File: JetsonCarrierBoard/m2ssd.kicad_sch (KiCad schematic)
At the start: 0 parts

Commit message: Finished First Design of M.2 SSD wiring
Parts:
- added C? (x8): 0.22u, symbol Device:C
- added J?: Bus_M.2_Socket_M, symbol Connector:Bus_M.2_Socket_M
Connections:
- new net: C?.2, J?.25 (PETp2)
- new net: C?.2, J?.11 (PETn3)
- new net: C?.2, J?.35 (PETn1)
- new net: C?.2, J?.47 (PETn0/SATA-A-)
- new net: C?.2, J?.13 (PETp3)
- new net: C?.2, J?.23 (PETn2)
- new net: C?.2, J?.37 (PETp1)
- new net: C?.2, J?.49 (PETp0/SATA-A+)
- new net +3.3V: J?.12 (3.3V), J?.14 (3.3V), J?.16 (3.3V), J?.18 (3.3V), J?.2 (3.3V), J?.4 (3.3V), J?.70 (3.3V), J?.72 (3.3V), J?.74 (3.3V)
- new net GND: J?.1 (GND), J?.15 (GND), J?.21 (GND), J?.27 (GND), J?.3 (GND), J?.33 (GND), J?.39 (GND), J?.45 (GND), J?.51 (GND), J?.57 (GND), J?.71 (GND), J?.73 (GND), J?.75 (GND), J?.9 (GND)
- new net PCIE0_CLKREQ: J?.52 (~{CLKREQ})
- new net PCIE0_CLK_N: J?.53 (REFCLKn)
- new net PCIE0_CLK_P: J?.55 (REFCLKp)
- new net PCIE0_RST: J?.50 (~{PERST})
- new net PCIE0_RX0_N: J?.41 (PERn0/SATA-B+)
- new net PCIE0_RX0_P: J?.43 (PERp0/SATA-B-)
- new net PCIE0_RX1_N: J?.29 (PERn1)
- new net PCIE0_RX1_P: J?.31 (PERp1)
- new net PCIE0_RX2_N: J?.17 (PERn2)
- new net PCIE0_RX2_P: J?.19 (PERp2)
- new net PCIE0_RX3_N: J?.5 (PERn3)
- new net PCIE0_RX3_P: J?.7 (PERp3)
- new net PCIE0_TX0_N: C?.1
- new net PCIE0_TX0_P: C?.1
- new net PCIE0_TX1_N: C?.1
- new net PCIE0_TX1_P: C?.1
- new net PCIE0_TX2_N: C?.1
- new net PCIE0_TX2_P: C?.1
- new net PCIE0_TX3_N: C?.1
- new net PCIE0_TX3_P: C?.1
- new net PCIE_WAKE: J?.54 (~{PEWAKE})
- no-connect marks 0 -> 3

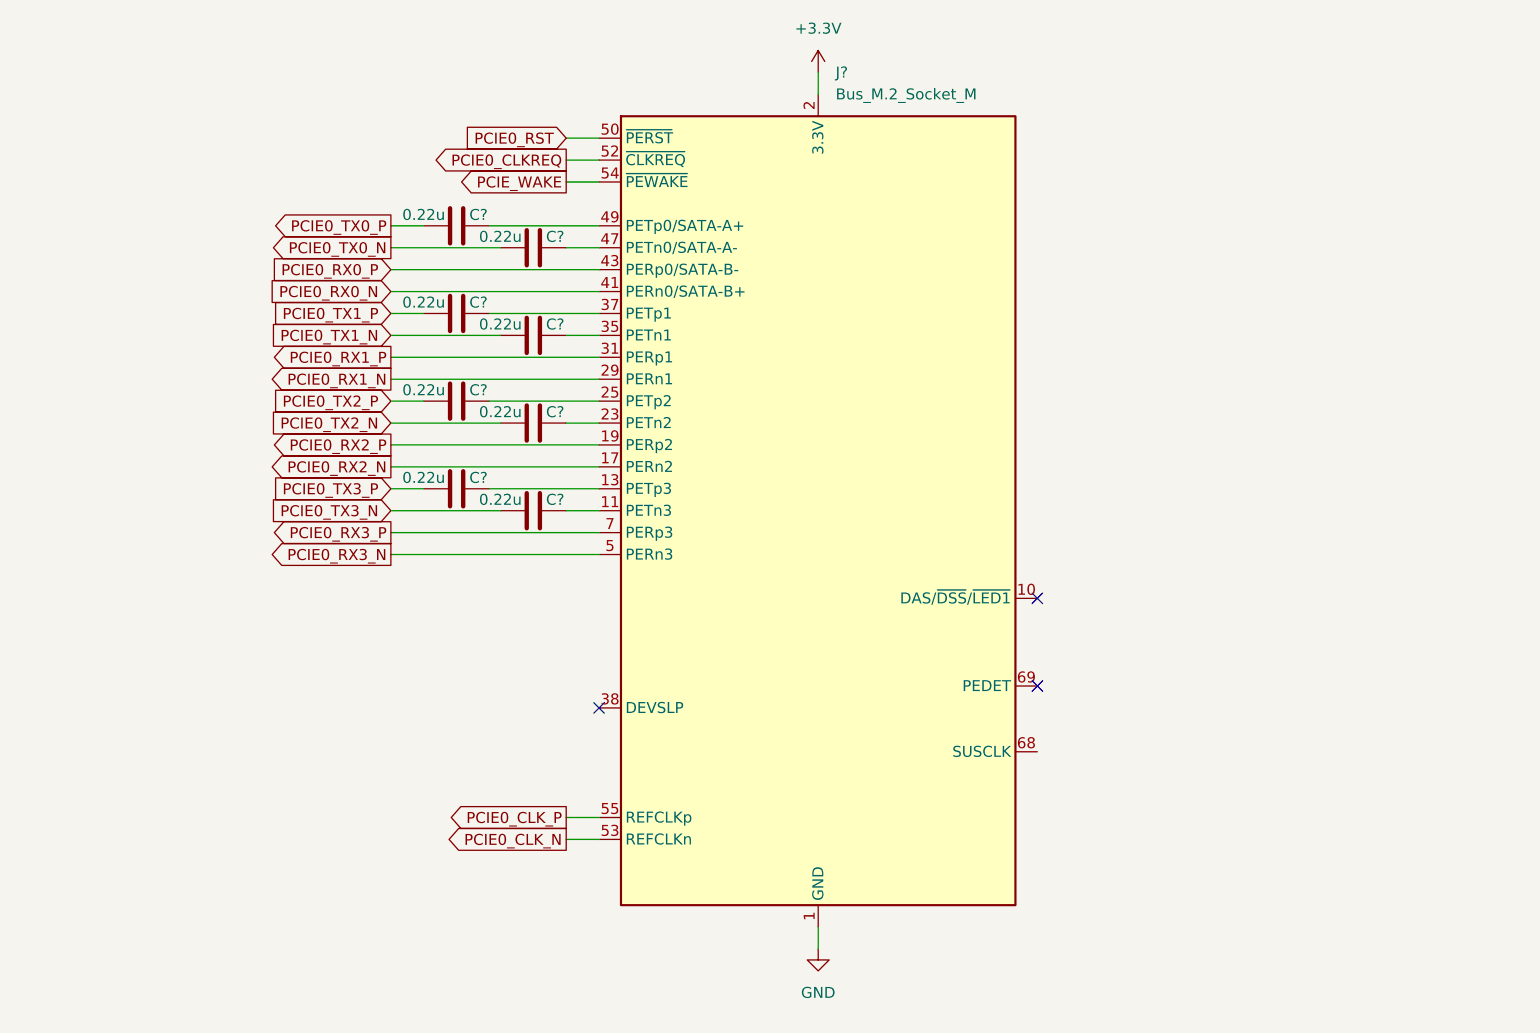
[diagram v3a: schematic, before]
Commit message: IMU wiring
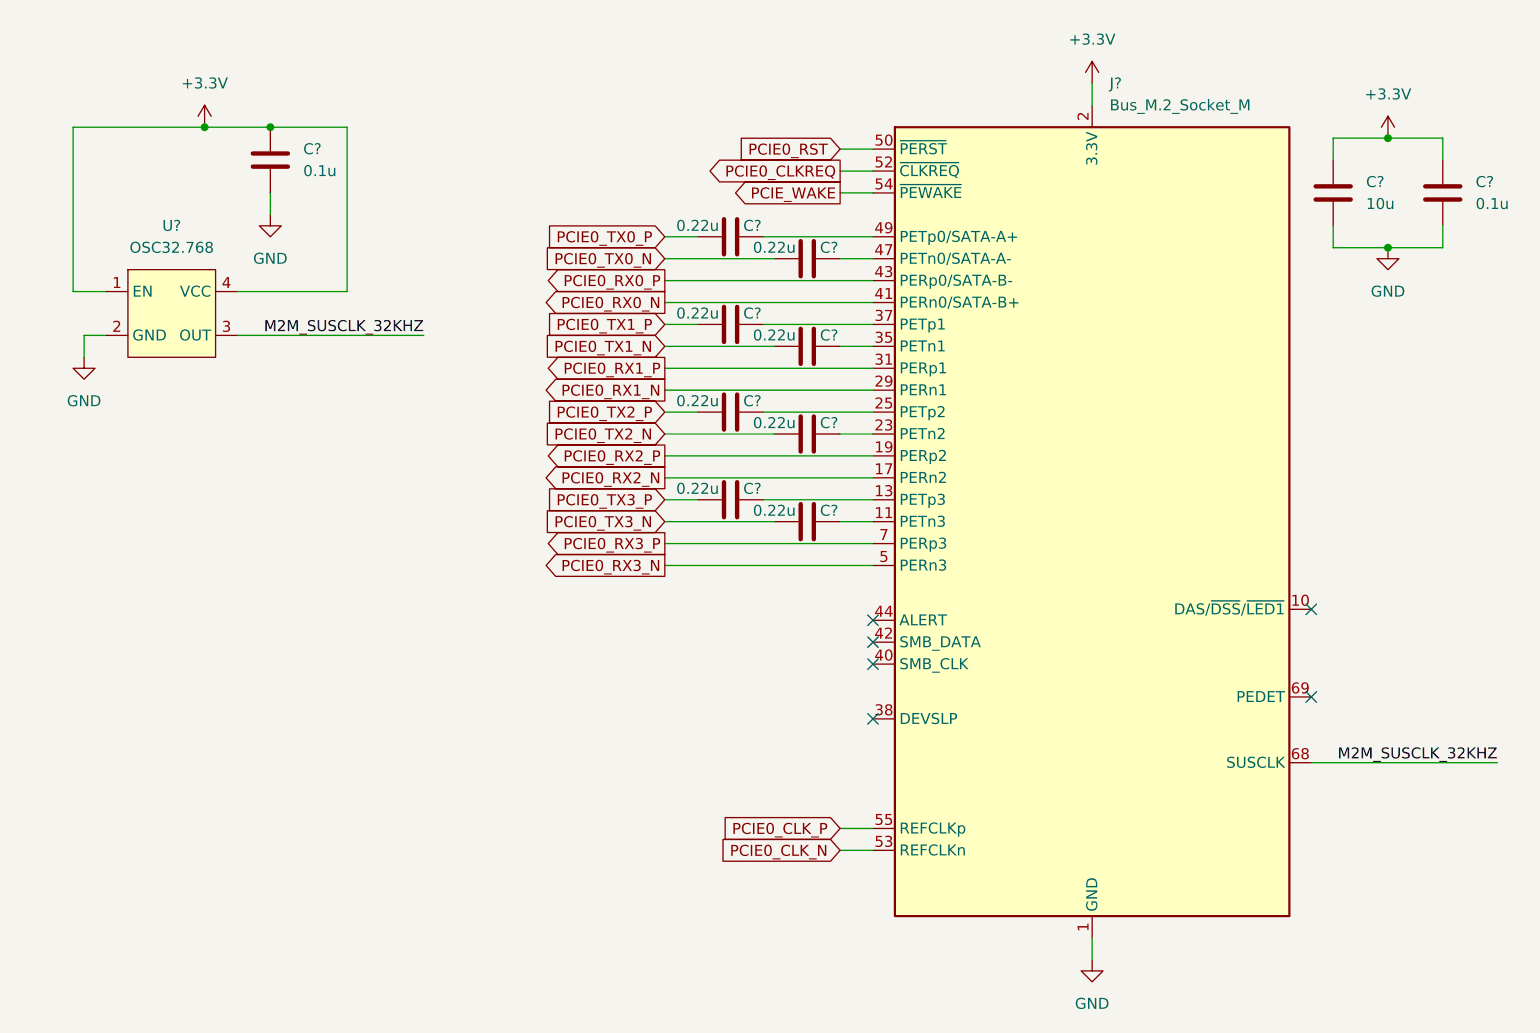
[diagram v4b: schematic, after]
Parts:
- added C? (x2): 0.1u, symbol Device:C
- added C?: 10u, symbol Device:C
- added U?: OSC32.768, symbol Crystals:OSC32.768
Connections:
- net +3.3V: now also C?.1, C?.1, C?.1, U?.1 (EN), U?.4 (VCC)
- net GND: now also C?.2, C?.2, C?.2, U?.2 (GND)
- net M2M_SUSCLK_32KHZ: now reaches J?.68 (SUSCLK)
- net M2M_SUSCLK_32KHZ: now also U?.3 (OUT)
- no-connect marks 3 -> 6
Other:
- moved on the sheet: C?

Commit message: Adding more Title block info and changing main hierarchical page layout
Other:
- title: (none) -> M.2 SSD (Key M)
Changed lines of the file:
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@@
 (kicad_sch (version 20211123) (generator eeschema)
   (paper "A4")
+  (title_block
+    (title "M.2 SSD (Key M)")
+    (date "2022-09-18")
+    (rev "1.0")
+  )
   (junction (at 215.9 54.61) (diameter 0) (color 0 0 0 0)
   )

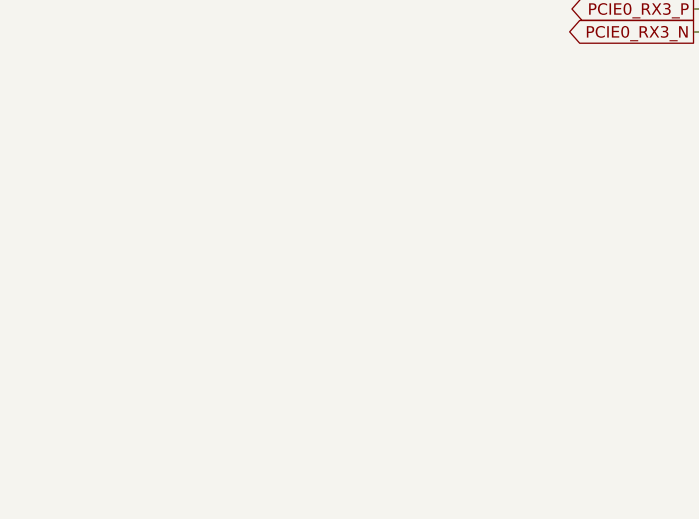
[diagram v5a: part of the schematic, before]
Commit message: Improvement list, fixes, and readability improvements
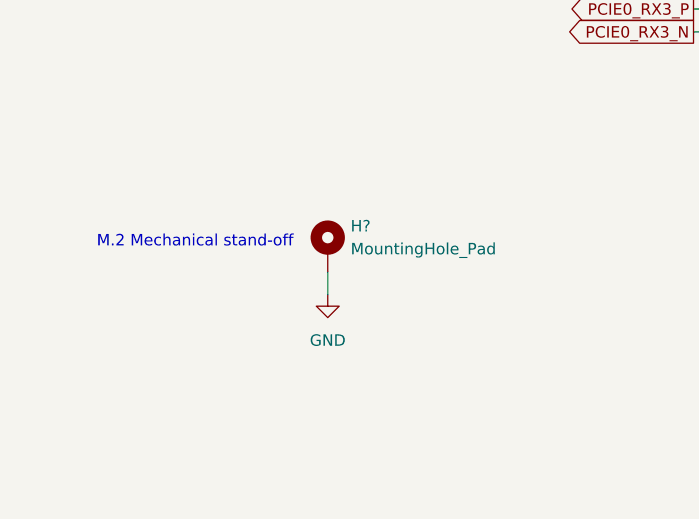
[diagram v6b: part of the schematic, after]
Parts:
- added H?: MountingHole_Pad, symbol Mechanical:MountingHole_Pad
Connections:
- net GND: now also H?.1
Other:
- note added: "M.2 Mechanical stand-off"
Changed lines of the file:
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@@
+    (stroke (width 0) (type default) (color 0 0 0 0))
+  )
+  (wire (pts (xy 91.44 130.81) (xy 91.44 133.35))
     (stroke (width 0) (type default) (color 0 0 0 0))
   )
@@
   (wire (pts (xy 209.55 67.31) (xy 215.9 67.31))
     (stroke (width 0) (type default) (color 0 0 0 0))
+  )
+  (text "M.2 Mechanical stand-off" (at 87.63 128.27 180)
+    (effects (font (size 1.27 1.27)) (justify right bottom))
   )
   (label "M2M_SUSCLK_32KHZ" (at 228.6 127 180)
@@
       (effects (font (size 1.27 1.27)) (justify right) hide)
     )
+  )
+  (symbol (lib_id "Mechanical:MountingHole_Pad") (at 91.44 128.27 0) (unit 1)
+    (in_bom yes) (on_board yes) (fields_autoplaced)
+    (property "Reference" "H?" (id 0) (at 93.98 125.7299 0)
+      (effects (font (size 1.27 1.27)) (justify left))
+    )
+    (property "Value" "MountingHole_Pad" (id 1) (at 93.98 128.2699 0)
+      (effects (font (size 1.27 1.27)) (justify left))
+    )
+    (property "Footprint" "" (id 2) (at 91.44 128.27 0)
+      (effects (font (size 1.27 1.27)) hide)
+    )
+    (property "Datasheet" "~" (id 3) (at 91.44 128.27 0)
+      (effects (font (size 1.27 1.27)) hide)
+    )
+    (pin "1")
   )
   (symbol (lib_id "Crystals:OSC32.768") (at 74.93 69.85 0) (unit 1)
@@
     (pin "2")
   )
+  (symbol (lib_id "power:GND") (at 91.44 133.35 0) (unit 1)
+    (in_bom yes) (on_board yes) (fields_autoplaced)
+    (property "Reference" "#PWR?" (id 0) (at 91.44 139.7 0)
+      (effects (font (size 1.27 1.27)) hide)
+    )
+    (property "Value" "GND" (id 1) (at 91.44 138.43 0))
+    (property "Footprint" "" (id 2) (at 91.44 133.35 0)
+      (effects (font (size 1.27 1.27)) hide)
+    )
+    (property "Datasheet" "" (id 3) (at 91.44 133.35 0)
+      (effects (font (size 1.27 1.27)) hide)
+    )
+    (pin "1")
+  )
   (symbol (lib_id "Device:C") (at 86.36 57.15 0) (unit 1)
